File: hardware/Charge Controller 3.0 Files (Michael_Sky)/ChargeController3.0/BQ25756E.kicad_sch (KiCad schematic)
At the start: 16 parts, among them U1 BQ25756ERRVR

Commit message: New formatting
New formatting
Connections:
- net CE is gone; now on net GND: U1.7 (~{CE})
- net PGND is gone; now on net GND: U1.17 (PGND), U1.22 (PGND), U1.37 (PGND)
- net SYS/BATT renamed BATT_PIN
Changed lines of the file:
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@@
+	(wire
+		(pts
+			(xy 139.7 129.54) (xy 139.7 130.81)
+		)
+		(stroke
+			(width 0)
+			(type default)
+		)
+	)
 	(wire
 		(pts
@@
 	(wire
 		(pts
+			(xy 76.2 120.65) (xy 76.2 119.38)
+		)
+		(stroke
+			(width 0)
+			(type default)
+		)
+	)
+	(wire
+		(pts
 			(xy 213.36 83.82) (xy 217.17 83.82)
 		)
@@
 	(wire
 		(pts
+			(xy 76.2 119.38) (xy 81.28 119.38)
+		)
+		(stroke
+			(width 0)
+			(type default)
+		)
+	)
+	(wire
+		(pts
 			(xy 132.08 58.42) (xy 146.05 58.42)
 		)
@@
 		(pts
 			(xy 167.64 53.34) (xy 194.31 53.34)
-		)
-		(stroke
-			(width 0)
-			(type default)
-		)
-	)
-	(wire
-		(pts
-			(xy 78.74 119.38) (xy 81.28 119.38)
 		)
 		(stroke
@@
 		)
 	)
-	(global_label "SYS{slash}BATT"
+	(global_label "BATT_PIN"
 		(shape input)
 		(at 58.42 49.53 0)
@@
 		)
 		(property "Intersheetrefs" "${INTERSHEET_REFS}"
-			(at 70.5371 49.53 0)
+			(at 69.8719 49.53 0)
 			(hide yes)
 			(show_name no)
@@
 		)
 	)
-	(global_label "SOL"
+	(global_label "IN"
 		(shape input)
 		(at 158.75 53.34 180)
@@
 		)
 		(property "Intersheetrefs" "${INTERSHEET_REFS}"
-			(at 152.1967 53.34 0)
+			(at 153.8295 53.34 0)
 			(hide yes)
 			(show_name no)
@@
 		)
 	)
-	(global_label "PGND"
+	(global_label "HIDRV_2"
 		(shape input)
-		(at 139.7 129.54 0)
+		(at 134.62 93.98 0)
 		(fields_autoplaced yes)
 		(effects
@@
 		)
 		(property "Intersheetrefs" "${INTERSHEET_REFS}"
-			(at 147.8257 129.54 0)
-			(hide yes)
-			(show_name no)
-			(do_not_autoplace no)
-			(effects
-				(font
-					(size 1.27 1.27)
-				)
-				(justify left)
-			)
-		)
-	)
-	(global_label "HIDRV_2"
+			(at 145.3462 93.98 0)
+			(hide yes)
+			(show_name no)
+			(do_not_autoplace no)
+			(effects
+				(font
+					(size 1.27 1.27)
+				)
+				(justify left)
+			)
+		)
+	)
+	(global_label "DRV_SUP"
 		(shape input)
-		(at 134.62 93.98 0)
+		(at 154.94 91.44 270)
 		(fields_autoplaced yes)
 		(effects
@@
 				(size 1.27 1.27)
 			)
-			(justify left)
+			(justify right)
 		)
 		(property "Intersheetrefs" "${INTERSHEET_REFS}"
-			(at 145.3462 93.98 0)
-			(hide yes)
-			(show_name no)
-			(do_not_autoplace no)
-			(effects
-				(font
-					(size 1.27 1.27)
-				)
-				(justify left)
-			)
-		)
-	)
-	(global_label "DRV_SUP"
+			(at 154.94 102.8314 90)
+			(hide yes)
+			(show_name no)
+			(do_not_autoplace no)
+			(effects
+				(font
+					(size 1.27 1.27)
+				)
+				(justify right)
+			)
+		)
+	)
+	(global_label "STAT_1"
 		(shape input)
-		(at 154.94 91.44 270)
+		(at 134.62 78.74 0)
 		(fields_autoplaced yes)
 		(effects
@@
 				(size 1.27 1.27)
 			)
-			(justify right)
-		)
-		(property "Intersheetrefs" "${INTERSHEET_REFS}"
-			(at 154.94 102.8314 90)
-			(hide yes)
-			(show_name no)
-			(do_not_autoplace no)
-			(effects
-				(font
-					(size 1.27 1.27)
-				)
-				(justify right)
-			)
-		)
-	)
-	(global_label "STAT_1"
-		(shape input)
-		(at 134.62 78.74 0)
-		(fields_autoplaced yes)
-		(effects
-			(font
-				(size 1.27 1.27)
-			)
 			(justify left)
 		)
@@
 				)
 				(justify left)
-			)
-		)
-	)
-	(global_label "CE"
-		(shape input)
-		(at 78.74 119.38 180)
-		(fields_autoplaced yes)
-		(effects
-			(font
-				(size 1.27 1.27)
-			)
-			(justify right)
-		)
-		(property "Intersheetrefs" "${INTERSHEET_REFS}"
-			(at 73.3358 119.38 0)
-			(hide yes)
-			(show_name no)
-			(do_not_autoplace no)
-			(effects
-				(font
-					(size 1.27 1.27)
-				)
-				(justify right)
 			)
 		)
@@
 	(symbol
 		(lib_id "power:GND")
+		(at 76.2 120.65 0)
+		(unit 1)
+		(body_style 1)
+		(exclude_from_sim no)
+		(in_bom yes)
+		(on_board yes)
+		(in_pos_files yes)
+		(dnp no)
+		(property "Reference" "#PWR012"
+			(at 76.2 127 0)
+			(hide yes)
+			(show_name no)
+			(do_not_autoplace no)
+			(effects
+				(font
+					(size 1.27 1.27)
+				)
+			)
+		)
+		(property "Value" "GND"
+			(at 74.422 124.46 0)
+			(show_name no)
+			(do_not_autoplace no)
+			(effects
+				(font
+					(size 1.27 1.27)
+				)
+				(justify left)
+			)
+		)
+		(property "Footprint" ""
+			(at 76.2 120.65 0)
+			(hide yes)
+			(show_name no)
+			(do_not_autoplace no)
+			(effects
+				(font
+					(size 1.27 1.27)
+				)
+			)
+		)
+		(property "Datasheet" ""
+			(at 76.2 120.65 0)
+			(hide yes)
+			(show_name no)
+			(do_not_autoplace no)
+			(effects
+				(font
+					(size 1.27 1.27)
+				)
+			)
+		)
+		(property "Description" "Power symbol creates a global label with name \"GND\" , ground"
+			(at 76.2 120.65 0)
+			(hide yes)
+			(show_name no)
+			(do_not_autoplace no)
+			(effects
+				(font
+					(size 1.27 1.27)
+				)
+			)
+		)
+		(pin "1"
+		)
+		(instances
+			(project "ChargeController3.0"
+				(path "/a54826c2-d365-4450-b7a8-71945dba02c0/9cc11239-a5da-4d64-84b9-35bfc57c50fe"
+					(reference "#PWR012")
+					(unit 1)
+				)
+			)
+		)
+	)
+	(symbol
+		(lib_id "power:GND")
+		(at 139.7 130.81 0)
+		(unit 1)
+		(body_style 1)
+		(exclude_from_sim no)
+		(in_bom yes)
+		(on_board yes)
+		(in_pos_files yes)
+		(dnp no)
+		(fields_autoplaced yes)
+		(property "Reference" "#PWR032"
+			(at 139.7 137.16 0)
+			(hide yes)
+			(show_name no)
+			(do_not_autoplace no)
+			(effects
+				(font
+					(size 1.27 1.27)
+				)
+			)
+		)
+		(property "Value" "GND"
+			(at 139.7 135.89 0)
+			(show_name no)
+			(do_not_autoplace no)
+			(effects
+				(font
+					(size 1.27 1.27)
+				)
+			)
+		)
+		(property "Footprint" ""
+			(at 139.7 130.81 0)
+			(hide yes)
+			(show_name no)
+			(do_not_autoplace no)
+			(effects
+				(font
+					(size 1.27 1.27)
+				)
+			)
+		)
+		(property "Datasheet" ""
+			(at 139.7 130.81 0)
+			(hide yes)
+			(show_name no)
+			(do_not_autoplace no)
+			(effects
+				(font
+					(size 1.27 1.27)
+				)
+			)
+		)
+		(property "Description" "Power symbol creates a global label with name \"GND\" , ground"
+			(at 139.7 130.81 0)
+			(hide yes)
+			(show_name no)
+			(do_not_autoplace no)
+			(effects
+				(font
+					(size 1.27 1.27)
+				)
+			)
+		)
+		(pin "1"
+		)
+		(instances
+			(project "ChargeController3.0"
+				(path "/a54826c2-d365-4450-b7a8-71945dba02c0/9cc11239-a5da-4d64-84b9-35bfc57c50fe"
+					(reference "#PWR032")
+					(unit 1)
+				)
+			)
+		)
+	)
+	(symbol
+		(lib_id "power:GND")
 		(at 217.17 106.68 0)
 		(unit 1)
@@
 			)
 		)
-		(property "Description" ""
+		(property "Description" "Stand-alone or I²C-controlled bidirectional buck-boost charge controller for up to 7S batteries"
 			(at 106.68 88.9 0)
 			(hide yes)

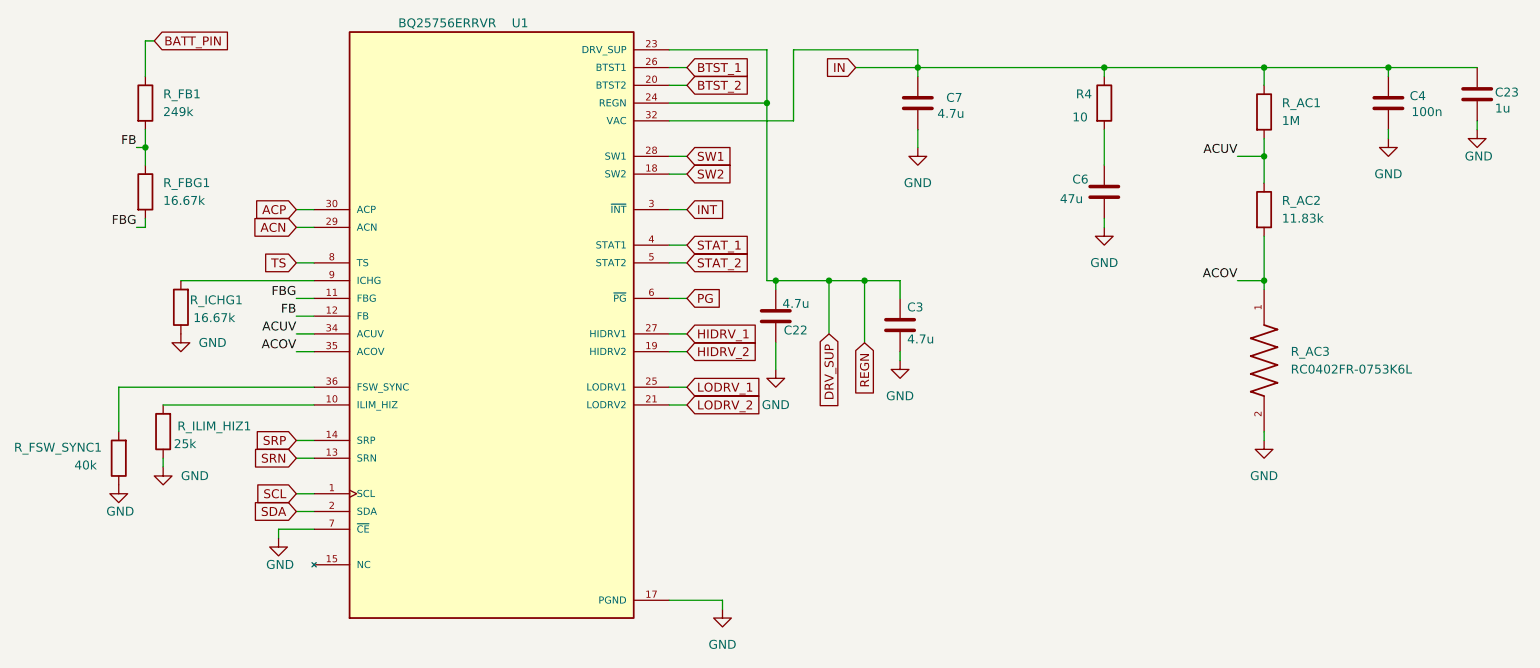
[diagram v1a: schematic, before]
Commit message: Final PCB?
inhibits rework, filtering rework
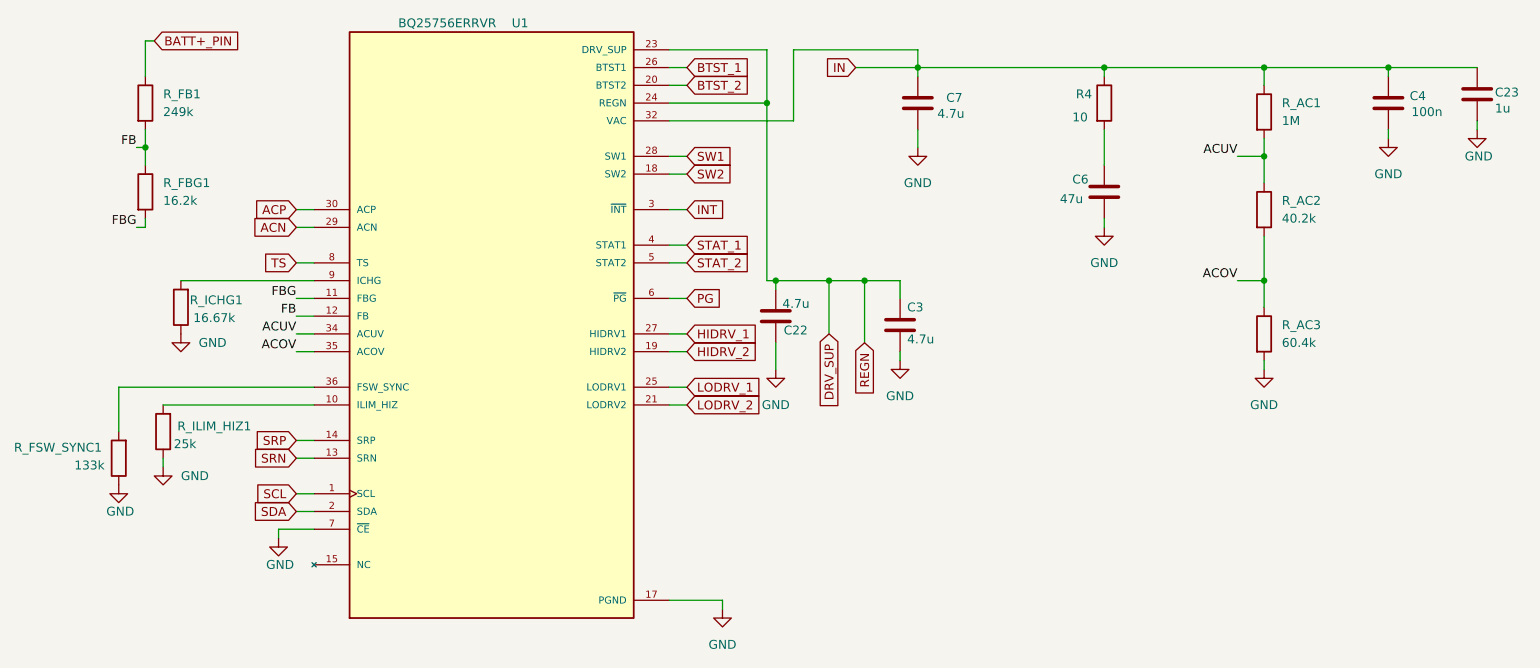
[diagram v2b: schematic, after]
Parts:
- removed R_AC3: RC0402FR-0753K6L, bmsfootprints:RC0402FR-0753K6L, symbol RC0402FR-0753K6L:RC0402FR-0753K6L
- added R_AC3: 60.4k, Resistor_SMD:R_0603_1608Metric, symbol Device:R
- R_AC2: value 11.83k -> 40.2k
- R_FBG1: value 16.67k -> 16.2k
- R_FSW_SYNC1: value 40k -> 133k; footprint Resistor_SMD:R_0402_1005Metric -> Resistor_SMD:R_0603_1608Metric
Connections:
- net ACOV: now also R_AC3.1
- net GND: now also R_AC3.2
- net BATT_PIN renamed BATT+_PIN
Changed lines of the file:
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@@
 	(wire
 		(pts
-			(xy 217.17 105.41) (xy 217.17 106.68)
+			(xy 217.17 95.25) (xy 217.17 96.52)
 		)
 		(stroke
@@
 	(wire
 		(pts
-			(xy 217.17 83.82) (xy 217.17 85.09)
+			(xy 217.17 83.82) (xy 217.17 87.63)
 		)
 		(stroke
@@
 		)
 	)
-	(global_label "BATT_PIN"
+	(global_label "BATT+_PIN"
 		(shape input)
 		(at 58.42 49.53 0)
@@
 		)
 		(property "Intersheetrefs" "${INTERSHEET_REFS}"
-			(at 69.8719 49.53 0)
+			(at 71.4443 49.53 0)
 			(hide yes)
 			(show_name no)
@@
 			)
 		)
-		(property "Value" "11.83k"
+		(property "Value" "40.2k"
 			(at 219.71 74.9299 0)
 			(show_name no)
@@
 	)
 	(symbol
-		(lib_id "RC0402FR-0753K6L:RC0402FR-0753K6L")
-		(at 217.17 95.25 270)
-		(unit 1)
-		(body_style 1)
-		(exclude_from_sim no)
-		(in_bom yes)
-		(on_board yes)
-		(in_pos_files yes)
-		(dnp no)
-		(fields_autoplaced yes)
-		(property "Reference" "R_AC3"
-			(at 220.98 93.9799 90)
-			(show_name no)
-			(do_not_autoplace no)
-			(effects
-				(font
-					(size 1.27 1.27)
-				)
-				(justify left)
-			)
-		)
-		(property "Value" "RC0402FR-0753K6L"
-			(at 220.98 96.5199 90)
-			(show_name no)
-			(do_not_autoplace no)
-			(effects
-				(font
-					(size 1.27 1.27)
-				)
-				(justify left)
-			)
-		)
-		(property "Footprint" "bmsfootprints:RC0402FR-0753K6L"
-			(at 217.17 95.25 0)
-			(hide yes)
-			(show_name no)
-			(do_not_autoplace no)
-			(effects
-				(font
-					(size 1.27 1.27)
-				)
-				(justify bottom)
-			)
-		)
-		(property "Datasheet" ""
-			(at 217.17 95.25 0)
-			(hide yes)
-			(show_name no)
-			(do_not_autoplace no)
-			(effects
-				(font
-					(size 1.27 1.27)
-				)
-			)
-		)
-		(property "Description" ""
-			(at 217.17 95.25 0)
-			(hide yes)
-			(show_name no)
-			(do_not_autoplace no)
-			(effects
-				(font
-					(size 1.27 1.27)
-				)
-			)
-		)
-		(pin "2"
-		)
-		(pin "1"
-		)
-		(instances
-			(project "ChargeController3.0"
-				(path "/a54826c2-d365-4450-b7a8-71945dba02c0/9cc11239-a5da-4d64-84b9-35bfc57c50fe"
-					(reference "R_AC3")
-					(unit 1)
-				)
-			)
-		)
-	)
-	(symbol
 		(lib_id "Device:C")
 		(at 234.95 58.42 0)
@@
 	(symbol
 		(lib_id "power:GND")
-		(at 217.17 106.68 0)
+		(at 217.17 96.52 0)
 		(unit 1)
 		(body_style 1)
@@
 		(fields_autoplaced yes)
 		(property "Reference" "#PWR010"
-			(at 217.17 113.03 0)
+			(at 217.17 102.87 0)
 			(hide yes)
 			(show_name no)
@@
 		)
 		(property "Value" "GND"
-			(at 217.17 111.76 0)
+			(at 217.17 101.6 0)
 			(show_name no)
 			(do_not_autoplace no)
@@
 		)
 		(property "Footprint" ""
-			(at 217.17 106.68 0)
+			(at 217.17 96.52 0)
 			(hide yes)
 			(show_name no)
@@
 		)
 		(property "Datasheet" ""
-			(at 217.17 106.68 0)
+			(at 217.17 96.52 0)
 			(hide yes)
 			(show_name no)
@@
 		)
 		(property "Description" "Power symbol creates a global label with name \"GND\" , ground"
-			(at 217.17 106.68 0)
+			(at 217.17 96.52 0)
 			(hide yes)
 			(show_name no)
@@
 			)
 		)
-		(property "Value" "40k"
+		(property "Value" "133k"
 			(at 46.99 110.236 0)
 			(show_name no)
@@
 			)
 		)
-		(property "Footprint" "Resistor_SMD:R_0402_1005Metric"
+		(property "Footprint" "Resistor_SMD:R_0603_1608Metric"
 			(at 55.118 109.22 90)
 			(hide yes)
@@
 			)
 		)
-		(property "Value" "16.67k"
+		(property "Value" "16.2k"
 			(at 59.69 72.3899 0)
 			(show_name no)
@@
 					(unit 1)
 				)
+			)
+		)
+	)
+	(symbol
+		(lib_id "Device:R")
+		(at 217.17 91.44 0)
+		(unit 1)
+		(body_style 1)
+		(exclude_from_sim no)
+		(in_bom yes)
+		(on_board yes)
+		(in_pos_files yes)
+		(dnp no)
+		(fields_autoplaced yes)
+		(property "Reference" "R_AC3"
+			(at 219.71 90.1699 0)
+			(show_name no)
+			(do_not_autoplace no)
+			(effects
+				(font
+					(size 1.27 1.27)
+				)
+				(justify left)
+			)
+		)
+		(property "Value" "60.4k"
+			(at 219.71 92.7099 0)
+			(show_name no)
+			(do_not_autoplace no)
+			(effects
+				(font
+					(size 1.27 1.27)
+				)
+				(justify left)
+			)
+		)
+		(property "Footprint" "Resistor_SMD:R_0603_1608Metric"
+			(at 215.392 91.44 90)
+			(hide yes)
+			(show_name no)
+			(do_not_autoplace no)
+			(effects
+				(font
+					(size 1.27 1.27)
+				)
+			)
+		)
+		(property "Datasheet" ""
+			(at 217.17 91.44 0)
+			(hide yes)
+			(show_name no)
+			(do_not_autoplace no)
+			(effects
+				(font
+					(size 1.27 1.27)
+				)
+			)
+		)
+		(property "Description" "Resistor"
+			(at 217.17 91.44 0)
+			(hide yes)
+			(show_name no)
+			(do_not_autoplace no)
+			(effects
+				(font
+					(size 1.27 1.27)
+				)
+			)
+		)
+		(pin "2"
+		)
+		(pin "1"
+		)
+		(instances
+			(project "ChargeController3.0"
+				(path "/a54826c2-d365-4450-b7a8-71945dba02c0/9cc11239-a5da-4d64-84b9-35bfc57c50fe"
+					(reference "R_AC3")
+					(unit 1)
+				)

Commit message: Sims + Gerbers added
Sims + Gerbers added
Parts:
- C6: value 47u -> 1u
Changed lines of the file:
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@@
 			)
 		)
-		(property "Value" "47u"
+		(property "Value" "1u"
 			(at 187.96 72.136 0)
 			(show_name no)
